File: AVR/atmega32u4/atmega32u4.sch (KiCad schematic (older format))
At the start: 11 parts

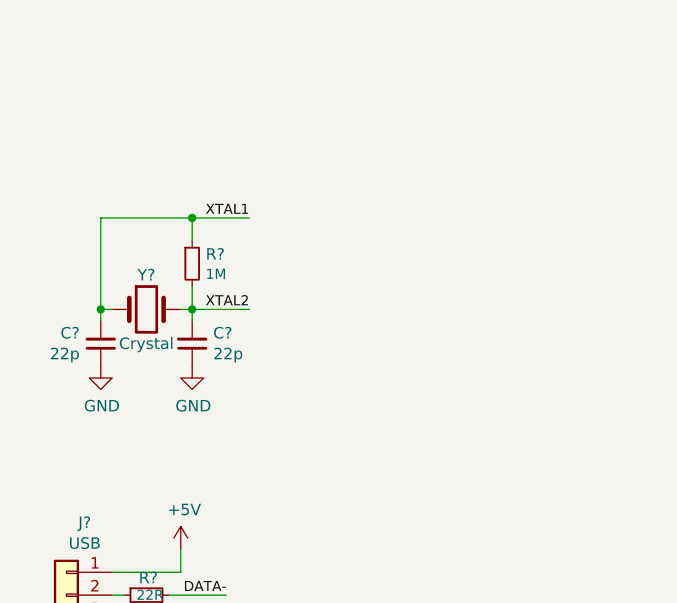
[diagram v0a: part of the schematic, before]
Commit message: Improving AVR templates
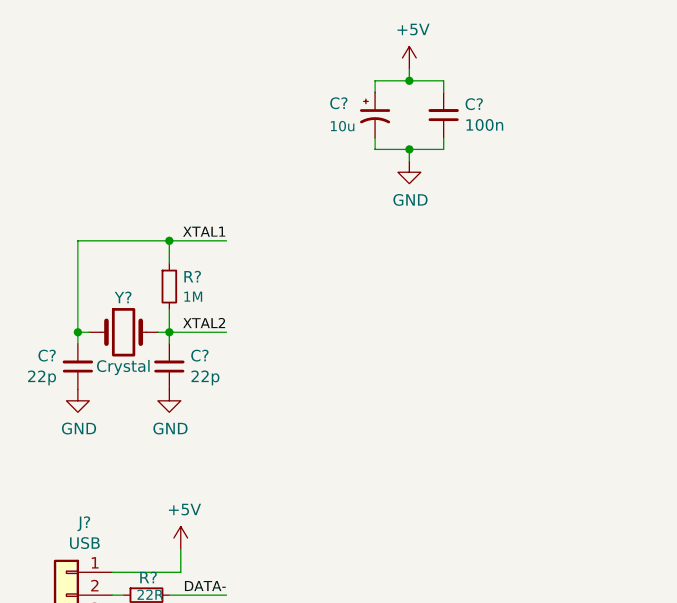
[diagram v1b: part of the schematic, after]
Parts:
- added C?: 100n, symbol Device:C_Small
- added C?: 10u, symbol Device:CP1_Small
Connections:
- net +5V: now also C?.1, C?.2
- net GND: now also C?.1, C?.2
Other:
- moved on the sheet: C?, R?, Y?
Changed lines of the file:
@@
 EESchema Schematic File Version 4
-LIBS:atmega32u2-cache
+LIBS:atmega32u4-cache
 EELAYER 26 0
 EELAYER END
@@
 $EndDescr
 Wire Wire Line
-	1900 2550 1850 2550
-Wire Wire Line
-	2250 2450 2250 2550
-Connection ~ 2250 2550
-Connection ~ 1850 2550
-Wire Wire Line
-	2200 2550 2250 2550
-Text Label 2500 2150 2    44   ~ 0
+	1800 2650 1750 2650
+Wire Wire Line
+	2150 2550 2150 2650
+Connection ~ 2150 2650
+Connection ~ 1750 2650
+Wire Wire Line
+	2100 2650 2150 2650
+Text Label 2400 2250 2    44   ~ 0
 XTAL1
-Text Label 2500 2550 2    44   ~ 0
+Text Label 2400 2650 2    44   ~ 0
 XTAL2
 Wire Wire Line
-	1850 2150 1850 2550
-Wire Wire Line
-	2500 2150 2250 2150
-Wire Wire Line
-	2250 2250 2250 2150
-Connection ~ 2250 2150
-Wire Wire Line
-	2250 2550 2250 2600
-Wire Wire Line
-	2250 2550 2500 2550
-Wire Wire Line
-	1850 2550 1850 2600
-Wire Wire Line
-	2250 2150 1850 2150
+	1750 2250 1750 2650
+Wire Wire Line
+	2400 2250 2150 2250
+Wire Wire Line
+	2150 2350 2150 2250
+Connection ~ 2150 2250
+Wire Wire Line
+	2150 2650 2150 2700
+Wire Wire Line
+	2150 2650 2400 2650
+Wire Wire Line
+	1750 2650 1750 2700
+Wire Wire Line
+	2150 2250 1750 2250
 $Comp
 L Device:Crystal Y?
 U 1 1 5B7974AC
-P 2050 2550
-F 0 "Y?" H 2050 2700 50  0000 C CNN
-F 1 "Crystal" H 2050 2400 50  0000 C CNN
-F 2 "" H 2050 2550 50  0001 C CNN
-F 3 "~" H 2050 2550 50  0001 C CNN
-	1    2050 2550
+P 1950 2650
+F 0 "Y?" H 1950 2800 50  0000 C CNN
+F 1 "Crystal" H 1950 2500 50  0000 C CNN
+F 2 "" H 1950 2650 50  0001 C CNN
+F 3 "~" H 1950 2650 50  0001 C CNN
+	1    1950 2650
 	1    0    0    -1
 $EndComp
@@
 L power:GND #PWR?
 U 1 1 5B79740B
-P 1850 2800
-F 0 "#PWR?" H 1850 2550 50  0001 C CNN
-F 1 "GND" H 1855 2627 50  0000 C CNN
-F 2 "" H 1850 2800 50  0001 C CNN
-F 3 "" H 1850 2800 50  0001 C CNN
-	1    1850 2800
+P 1750 2900
+F 0 "#PWR?" H 1750 2650 50  0001 C CNN
+F 1 "GND" H 1755 2727 50  0000 C CNN
+F 2 "" H 1750 2900 50  0001 C CNN
+F 3 "" H 1750 2900 50  0001 C CNN
+	1    1750 2900
 	1    0    0    -1
 $EndComp
@@
 L Device:C_Small C?
 U 1 1 5B7975FD
-P 1850 2700
-F 0 "C?" H 1758 2654 50  0000 R CNN
-F 1 "22p" H 1758 2745 50  0000 R CNN
-F 2 "" H 1850 2700 50  0001 C CNN
-F 3 "~" H 1850 2700 50  0001 C CNN
-	1    1850 2700
+P 1750 2800
+F 0 "C?" H 1658 2754 50  0000 R CNN
+F 1 "22p" H 1658 2845 50  0000 R CNN
+F 2 "" H 1750 2800 50  0001 C CNN
+F 3 "~" H 1750 2800 50  0001 C CNN
+	1    1750 2800
 	1    0    0    1
 $EndComp
@@
 L Device:C_Small C?
 U 1 1 5B7979A7
-P 2250 2700
-F 0 "C?" H 2158 2654 50  0000 R CNN
-F 1 "22p" H 2158 2745 50  0000 R CNN
-F 2 "" H 2250 2700 50  0001 C CNN
-F 3 "~" H 2250 2700 50  0001 C CNN
-	1    2250 2700
+P 2150 2800
+F 0 "C?" H 2058 2754 50  0000 R CNN
+F 1 "22p" H 2058 2845 50  0000 R CNN
+F 2 "" H 2150 2800 50  0001 C CNN
+F 3 "~" H 2150 2800 50  0001 C CNN
+	1    2150 2800
 	-1   0    0    1
 $EndComp
@@
 L power:GND #PWR?
 U 1 1 5B797A2C
-P 2250 2800
-F 0 "#PWR?" H 2250 2550 50  0001 C CNN
-F 1 "GND" H 2255 2627 50  0000 C CNN
-F 2 "" H 2250 2800 50  0001 C CNN
-F 3 "" H 2250 2800 50  0001 C CNN
-	1    2250 2800
+P 2150 2900
+F 0 "#PWR?" H 2150 2650 50  0001 C CNN
+F 1 "GND" H 2155 2727 50  0000 C CNN
+F 2 "" H 2150 2900 50  0001 C CNN
+F 3 "" H 2150 2900 50  0001 C CNN
+	1    2150 2900
 	1    0    0    -1
 $EndComp
@@
 L Device:R_Small R?
 U 1 1 5B797AEA
-P 2250 2350
-F 0 "R?" H 2309 2391 50  0000 L CNN
-F 1 "1M" H 2309 2304 44  0000 L CNN
-F 2 "" H 2250 2350 50  0001 C CNN
-F 3 "~" H 2250 2350 50  0001 C CNN
-	1    2250 2350
+P 2150 2450
+F 0 "R?" H 2209 2491 50  0000 L CNN
+F 1 "1M" H 2209 2404 44  0000 L CNN
+F 2 "" H 2150 2450 50  0001 C CNN
+F 3 "~" H 2150 2450 50  0001 C CNN
+	1    2150 2450
 	1    0    0    -1
 $EndComp
@@
 	1    0    0    -1
 $EndComp
+$Comp
+L Device:C_Small C?
+U 1 1 5B84BB74
+P 3350 1700
+F 0 "C?" H 3258 1654 50  0000 R CNN
+F 1 "100n" H 3258 1745 50  0000 R CNN
+F 2 "" H 3350 1700 50  0001 C CNN
+F 3 "~" H 3350 1700 50  0001 C CNN
+	1    3350 1700
+	-1   0    0    1
+$EndComp
+$Comp
+L power:GND #PWR?
+U 1 1 5B84BC7E
+P 3200 1900
+F 0 "#PWR?" H 3200 1650 50  0001 C CNN
+F 1 "GND" H 3205 1727 50  0000 C CNN
+F 2 "" H 3200 1900 50  0001 C CNN
+F 3 "" H 3200 1900 50  0001 C CNN
+	1    3200 1900
+	1    0    0    -1
+$EndComp
+$Comp
+L power:+5V #PWR?
+U 1 1 5B84BCA1
+P 3200 1500
+F 0 "#PWR?" H 3200 1350 50  0001 C CNN
+F 1 "+5V" H 3215 1673 50  0000 C CNN
+F 2 "" H 3200 1500 50  0001 C CNN
+F 3 "" H 3200 1500 50  0001 C CNN
+	1    3200 1500
+	1    0    0    -1
+$EndComp
+$Comp
+L Device:CP1_Small C?
+U 1 1 5B84BD33
+P 3050 1700
+F 0 "C?" H 2850 1750 50  0000 L CNN
+F 1 "10u" H 2850 1650 44  0000 L CNN
+F 2 "" H 3050 1700 50  0001 C CNN
+F 3 "~" H 3050 1700 50  0001 C CNN
+	1    3050 1700
+	1    0    0    -1
+$EndComp
+Wire Wire Line
+	3050 1800 3050 1850
+Wire Wire Line
+	3050 1850 3200 1850
+Wire Wire Line
+	3350 1850 3350 1800
+Wire Wire Line
+	3200 1850 3200 1900
+Connection ~ 3200 1850
+Wire Wire Line
+	3200 1850 3350 1850
+Wire Wire Line
+	3050 1600 3050 1550
+Wire Wire Line
+	3050 1550 3200 1550
+Wire Wire Line
+	3350 1550 3350 1600
+Wire Wire Line
+	3200 1550 3200 1500
+Connection ~ 3200 1550
+Wire Wire Line
+	3200 1550 3350 1550
 $EndSCHEMATC

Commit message: Update to KiCad 5.1.7
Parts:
- U?: symbol MCU_Microchip_ATmega:ATmega32U4-AU -> atmega32u4-rescue:ATmega32U4-AU-MCU_Microchip_ATmega
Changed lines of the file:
@@
 EESchema Schematic File Version 4
-LIBS:atmega32u4-cache
-EELAYER 26 0
+EELAYER 30 0
 EELAYER END
 $Descr A4 11693 8268
@@
 	2150 3900 2400 3900
 $Comp
-L MCU_Microchip_ATmega:ATmega32U4-AU U?
+L atmega32u4-rescue:ATmega32U4-AU-MCU_Microchip_ATmega U?
 U 1 1 5B843AD9
 P 6100 3675
